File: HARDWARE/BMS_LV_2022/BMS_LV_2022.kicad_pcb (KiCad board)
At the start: 4 copper layers, 90 x 45 mm, 166 parts, among them J1 Conn_01x06_Male, J11 Conn_01x07_Female, J2 Conn_01x12_Male, J3 USB_B_Mini, J4 Battery+, J5 Battery-, J6 Conn_01x09_Female, Q1 BC846, Q10 BSS138, Q11 SiSS05DN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

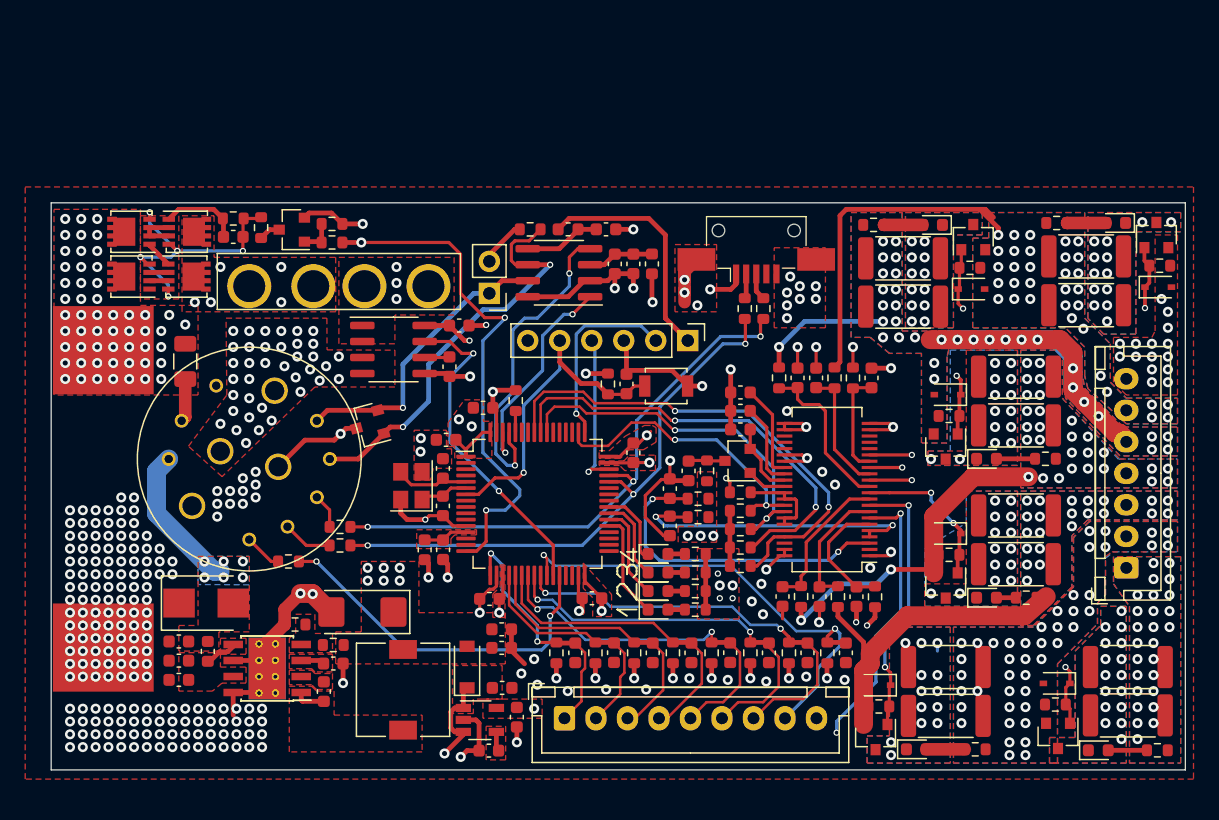
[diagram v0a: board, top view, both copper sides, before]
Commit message: Changes in V1.0
-Fuse holder change
-Autosport conn angle change
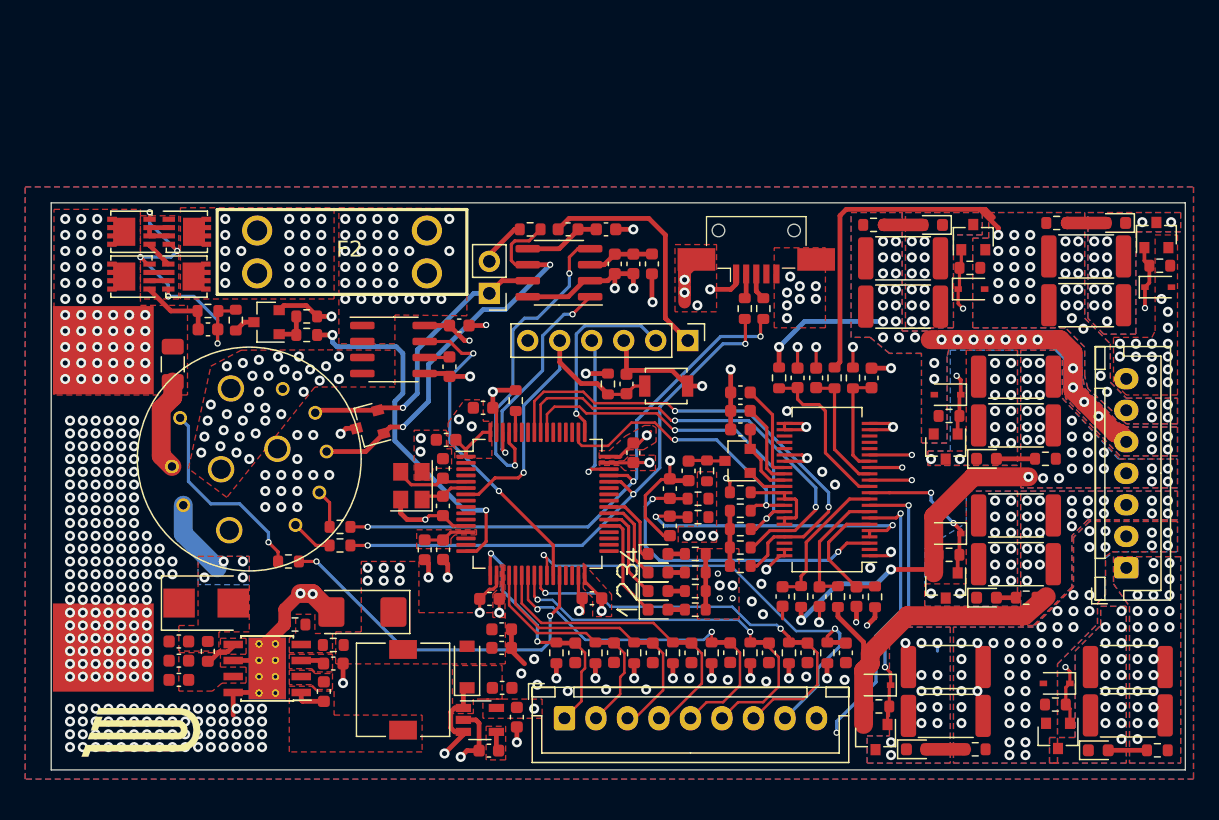
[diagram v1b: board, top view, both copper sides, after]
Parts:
- added G***: LOGO, Logos:PUTM_LOGO_11mm, F.Cu at (116.8, 121.9)
- F2: footprint footprints:Fuseholder_Keystone_3522-2 -> footprints:3557-2
- moved C41 7.61 mm to (122.4, 90.0)
- moved Q10 7.61 mm to (127.1, 89.5)
- moved R60 7.61 mm to (130.3, 89.0)
- moved R59 7.61 mm to (130.3, 90.5)
- moved R61 7.61 mm to (124.7, 89.3)
- moved R62 7.61 mm to (122.4, 88.6)
- moved F2 2.36 mm to (133.1, 83.9)
- moved F1 1.02 mm to (119.6, 92.8)
- turned J2 to 260 degrees
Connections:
- J2 pad 1: /CANH -> Net-(J2-Pad1)
- J2 pad 2: /CANL -> /CANH
- J2 pad 3: Net-(J2-Pad3) -> /CANL
- R13 pad 2: Net-(J2-Pad3) -> Net-(J2-Pad4)
- R14 pad 1: Net-(J2-Pad4) -> Net-(J2-Pad5)
- R15 pad 1: Net-(J2-Pad5) -> Net-(J2-Pad8)
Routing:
- net Net-(J2-Pad8): track 0.00 -> 15.9 mm, vias 0 -> 1
- net /Switch_Signal: track 40.8 -> 28.9 mm, vias 3 -> 2
- net GND: track 137.4 -> 130.8 mm, vias 257 -> 300
- net VCC: track 11.7 -> 6.09 mm, vias 6 -> 4
- net /VCC_Pin: track 3.43 -> 7.44 mm
- net Net-(J2-Pad3): track 2.77 -> 0.00 mm
- net /eFuse/Gate: track 23.4 -> 24.7 mm
- net Net-(J2-Pad4): track 3.96 -> 3.06 mm
- net Net-(F2-Pad2): vias 5 -> 21
- net /V_Out: vias 37 -> 32
- net /CS_IP+: vias 3 -> 30
- net +24V: vias 54 -> 48
- added copper zone on B.Cu, net GND
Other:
- board text added: "2022"
- board text added: "V1.0"

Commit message: Last Changes in V1.0
Fuse voltage measurement added
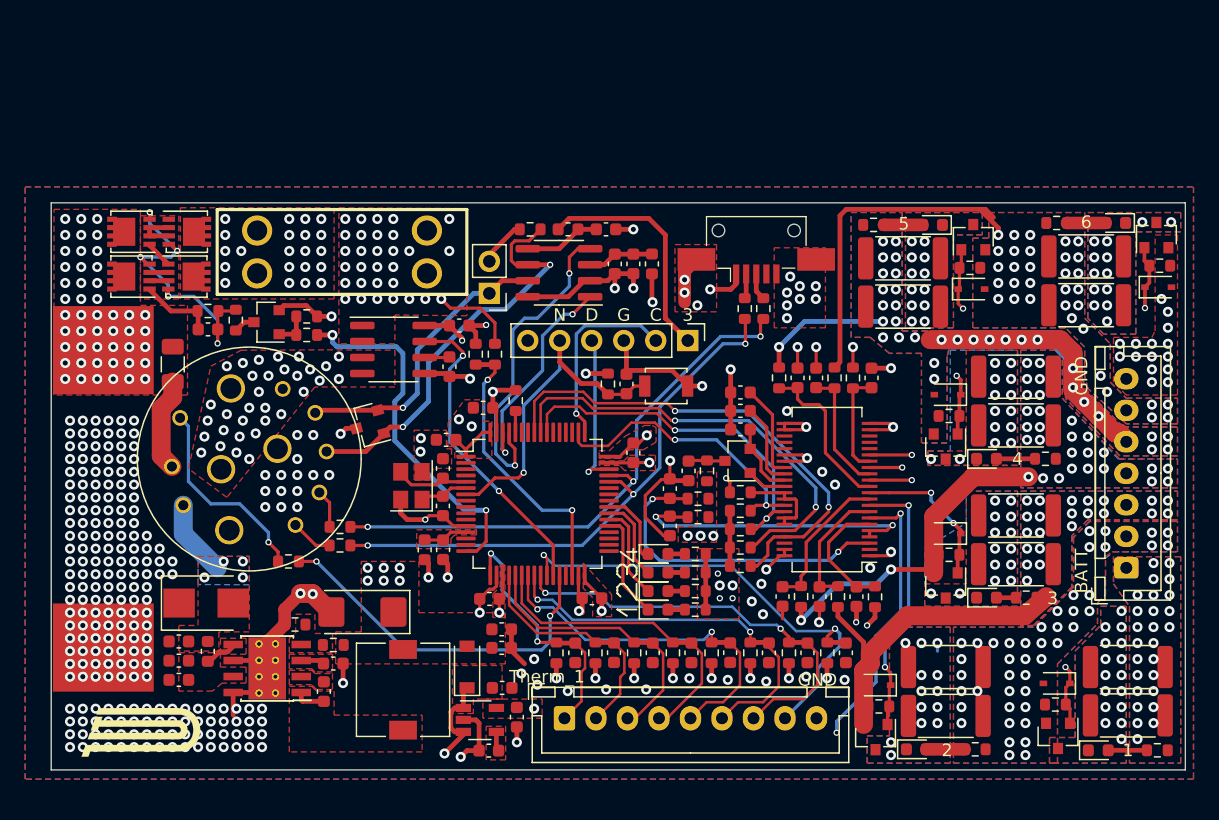
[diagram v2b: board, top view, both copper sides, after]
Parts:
- added R65: 20k, Resistor_SMD:R_0603_1608Metric, F.Cu at (145.2, 92.0)
- added R66: 2,7k, Resistor_SMD:R_0603_1608Metric, F.Cu at (143.7, 92.0)
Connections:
- U1 pad 30: Net-(U1-Pad30) -> /VoltageFuseMeasure
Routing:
- net /VoltageFuseMeasure: track 0.00 -> 22.9 mm, vias 0 -> 2
- net /CS_IP+: track 0.00 -> 6.70 mm
- net GND: track 130.8 -> 132.6 mm
- net /CurrentSensor_Out: track 26.0 -> 24.9 mm
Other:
- board text added: "1"
- board text added: "2"
- board text added: "3"
- board text added: "4"
- board text added: "5"
- board text added: "6"
- board text added: "C"
- board text added: "D"
- board text added: "G"
- board text added: "N"

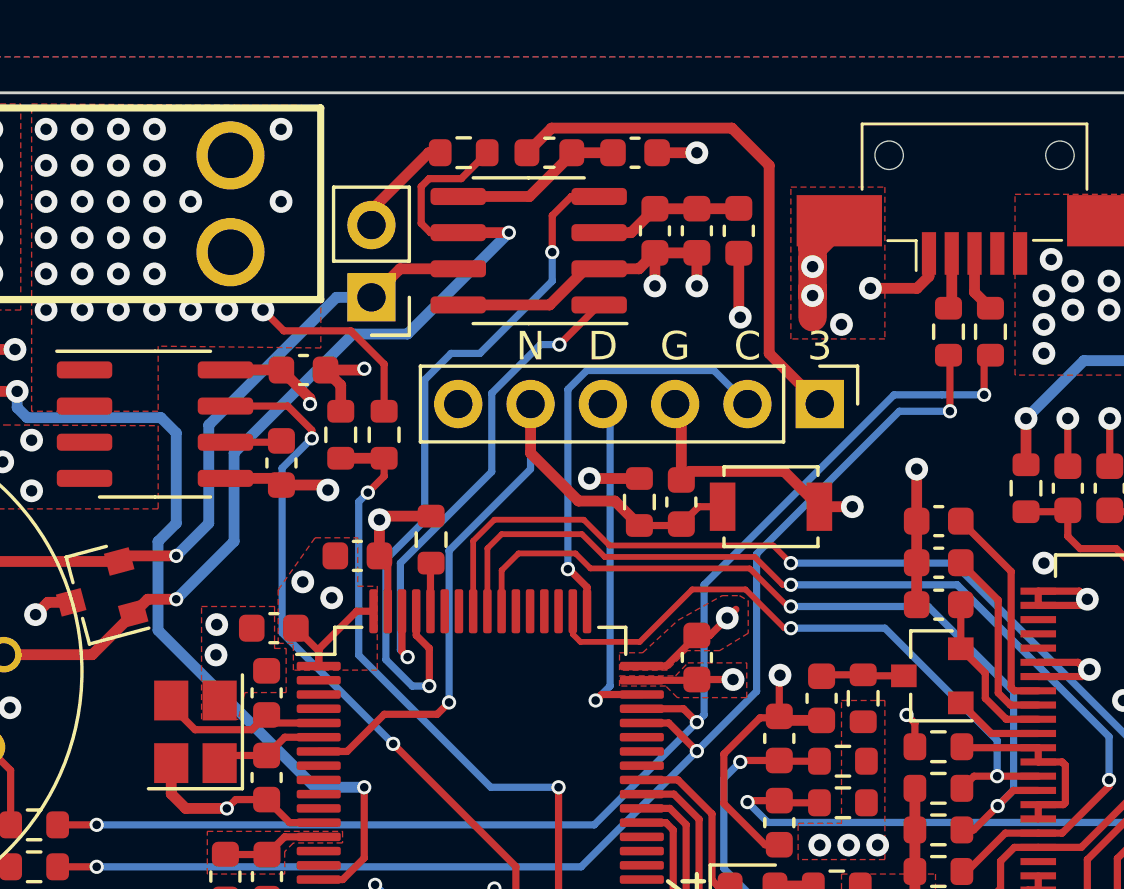
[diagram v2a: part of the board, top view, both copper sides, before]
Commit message: Voltage divider in current sensor section added
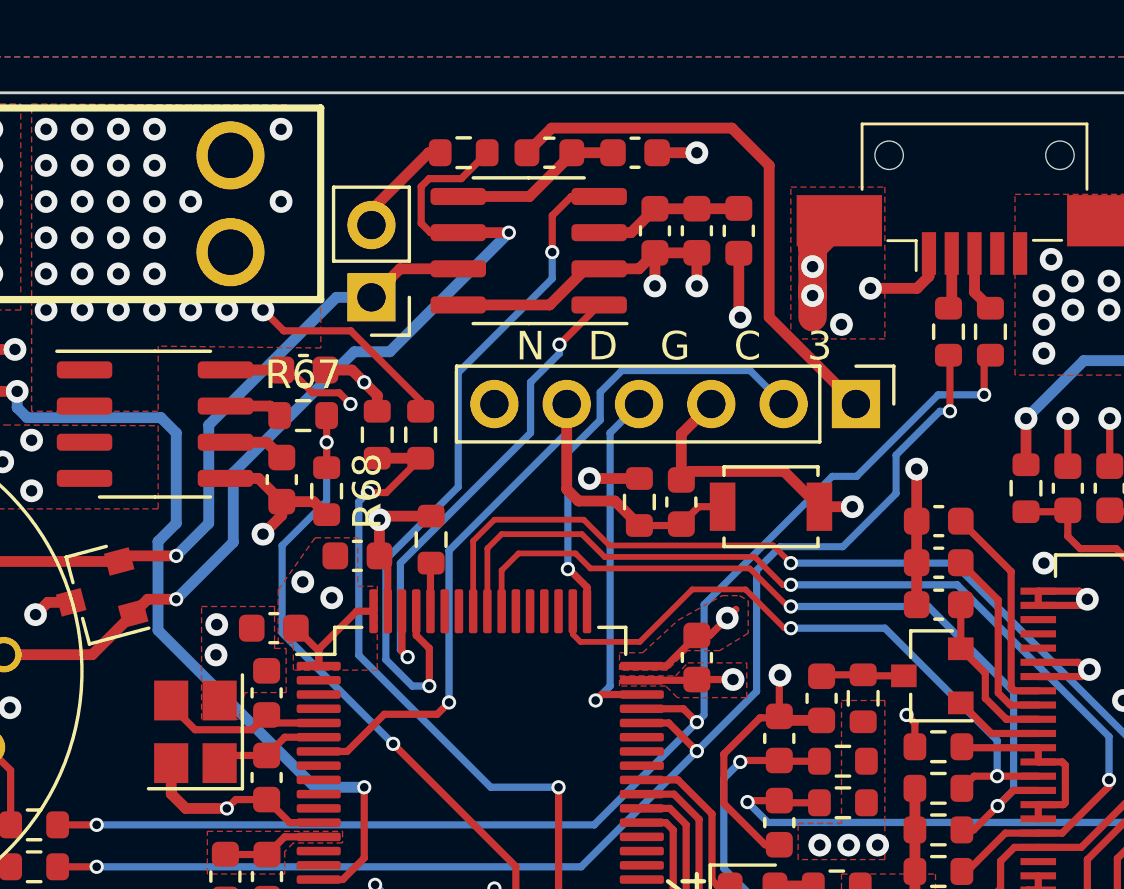
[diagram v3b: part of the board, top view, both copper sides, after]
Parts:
- added R67: 1k, Resistor_SMD:R_0603_1608Metric, F.Cu at (142.4, 91.3)
- added R68: 2k, Resistor_SMD:R_0603_1608Metric, F.Cu at (143.2, 94.0)
- Q2, Q3, Q4, Q5, Q6, Q7: value Q_NMOS_GSD -> ZXMN3F30FHTA
- R21, R22, R26, R27, R31, R32, R36, R37, R41, R42, R46, R47: value 30 -> 10
- moved R66 1.28 mm to (145.0, 92.0)
- moved R65 1.28 mm to (146.5, 92.0)
- moved J1 1.27 mm to (161.8, 90.9)
- moved C42 0.58 mm to (141.6, 93.6)
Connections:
- U5 pad 7: /CurrentSensor_Out -> Net-(R67-Pad1)
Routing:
- net Net-(R67-Pad1): track 0.00 -> 2.04 mm
- net /CurrentSensor_Out: track 24.9 -> 23.2 mm
- net GND: track 132.6 -> 134.2 mm
- net +5V: track 44.2 -> 45.5 mm
- net /VoltageFuseMeasure: track 22.9 -> 23.8 mm
- net /CAN-RX: track 25.3 -> 24.7 mm
- net /SW-CLK: track 15.2 -> 15.7 mm
- net /CS_IP+: track 6.70 -> 7.23 mm
- net +3V3: track 55.8 -> 56.3 mm

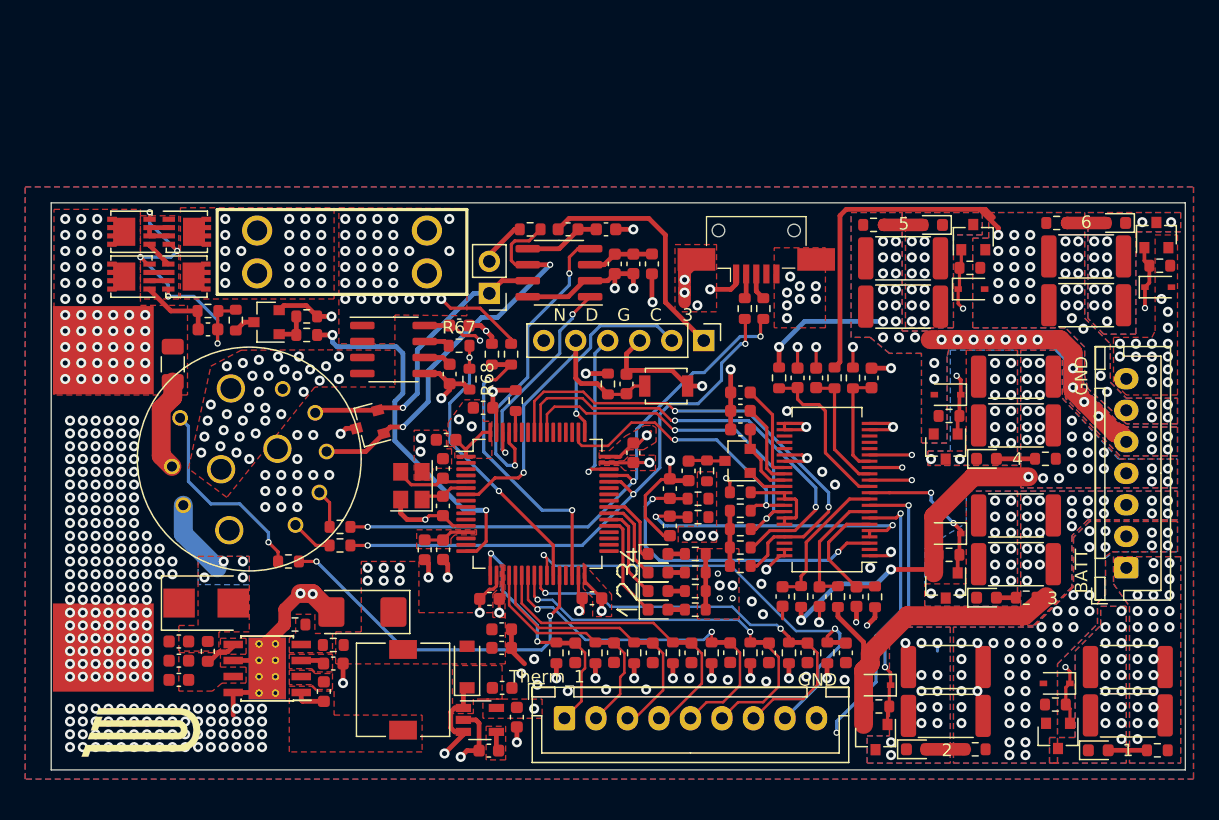
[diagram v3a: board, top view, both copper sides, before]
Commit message: Update project to KiCad 8.0
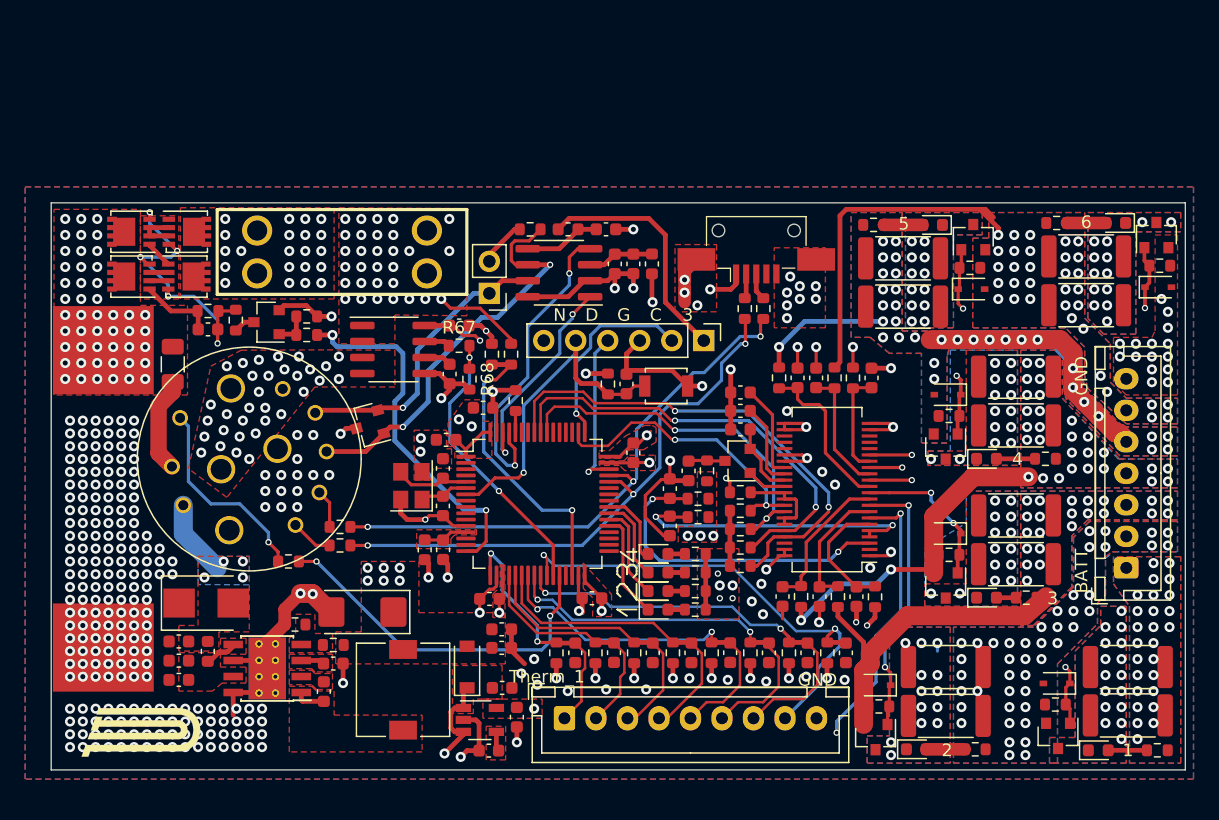
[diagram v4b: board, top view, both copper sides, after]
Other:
- net class Default removed
